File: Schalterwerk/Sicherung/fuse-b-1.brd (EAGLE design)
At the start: 20 x 54 mm, 19 parts, among them Q3 2SCR586D3

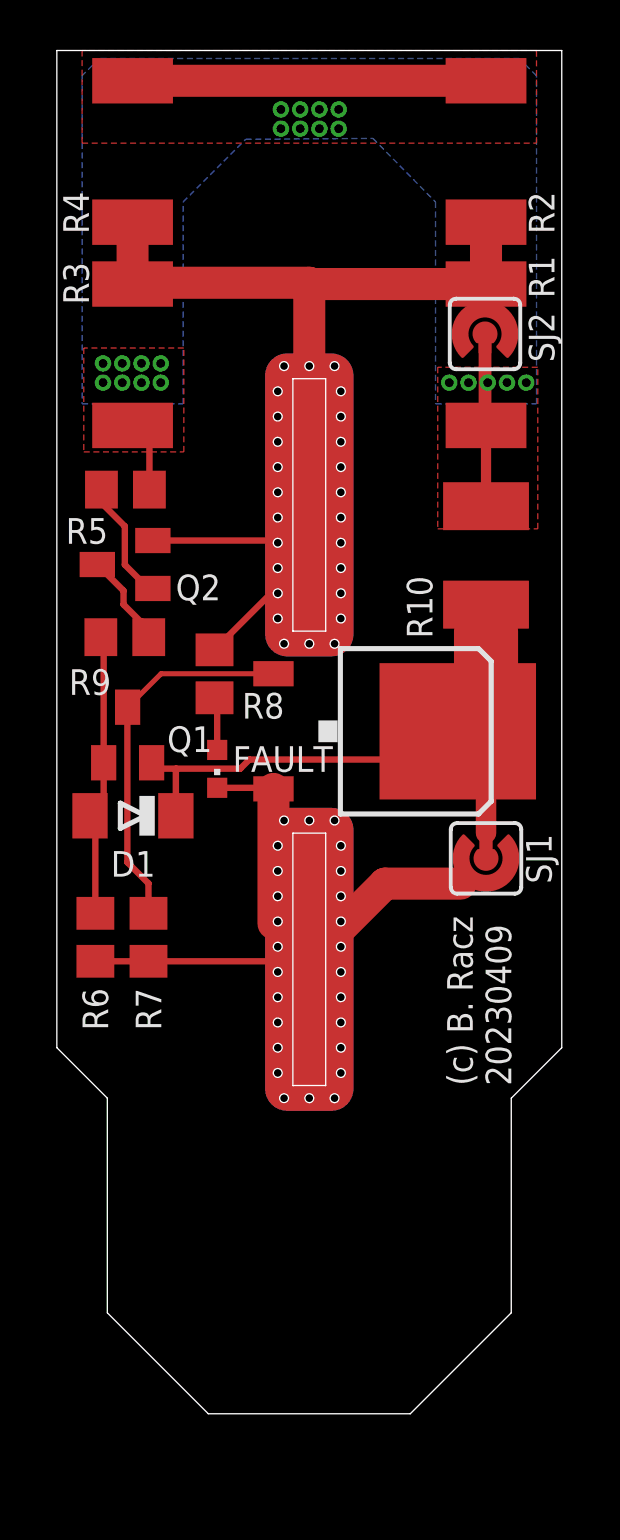
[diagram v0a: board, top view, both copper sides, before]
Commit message: Completes the layout of the fuse with blade inputs.
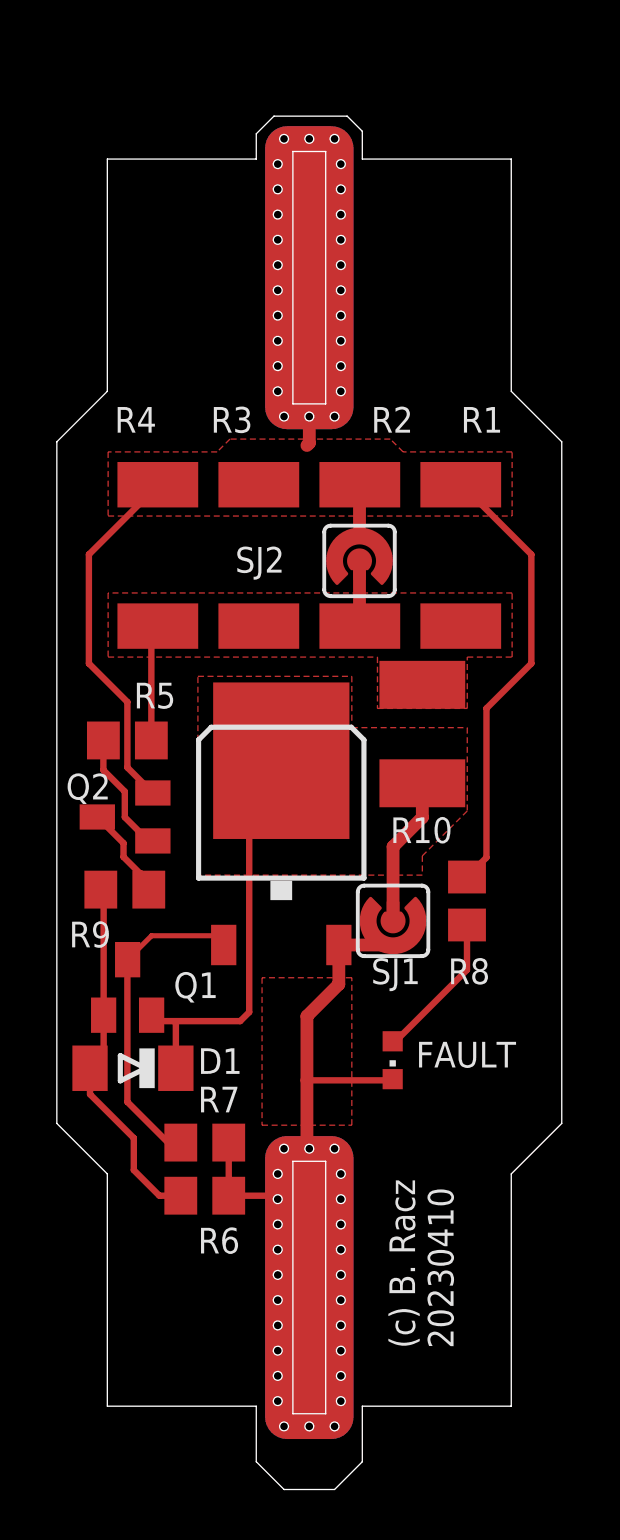
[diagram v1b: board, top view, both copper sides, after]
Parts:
- moved R2 16.8 mm to (12.0, 34.0), turned to 90 degrees
- moved R3 16.8 mm to (8.00, 34.0), turned to 90 degrees
- moved FAULT 13.5 mm to (13.3, 14.0)
- moved R8 13.5 mm to (16.2, 20.3)
- moved U$2 13.0 mm to (10.0, 5.00), flipped to the bottom, turned to 90 degrees
- moved R6 11.1 mm to (5.86, 8.64), turned to 180 degrees
- moved SJ2 10.3 mm to (12.0, 33.8)
- moved D1 10.0 mm to (3.01, 13.7)
- moved Q1 10.0 mm to (2.80, 16.9)
- moved Q2 10.0 mm to (2.70, 23.6)
- moved R9 10.0 mm to (2.69, 20.8)
- moved R5 9.94 mm to (2.79, 26.7)
- moved U$1 9.00 mm to (10.0, 45.0), flipped to the bottom, turned to 270 degrees
- moved R7 8.43 mm to (5.86, 10.7), turned to 180 degrees
- moved R1 8.01 mm to (16.0, 34.0)
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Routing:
- net FUSEIN: track 23.7 -> 8.28 mm, vias 21 -> 0
- net N$6: track 2.11 -> 5.89 mm
- net N$4: track 11.3 -> 14.4 mm
- net FUSEOUT: track 26.1 -> 23.2 mm
- net VIN: track 42.8 -> 40.9 mm
- net N$5: track 14.8 -> 13.0 mm
- net VOUT: track 26.3 -> 24.9 mm
- added copper zone on layer 1, net FUSEOUT
- added copper zone on layer 1, net VIN
- added copper zone on layer 1, net VOUT
- removed copper zone on layer 16, net FUSEIN
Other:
- board size 20 x 54 mm -> 20 x 54.4 mm
- board text added: "(c) B. Racz 20230410"
- board text removed: "(c) B. Racz 20230409"
